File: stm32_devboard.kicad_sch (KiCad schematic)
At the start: 26 parts, among them J1 Conn_01x04_Male, J2 USB_B_Micro, SW1 SW_SPDT, U2 STM32F103CBT6, Y1 Crystal_GND24

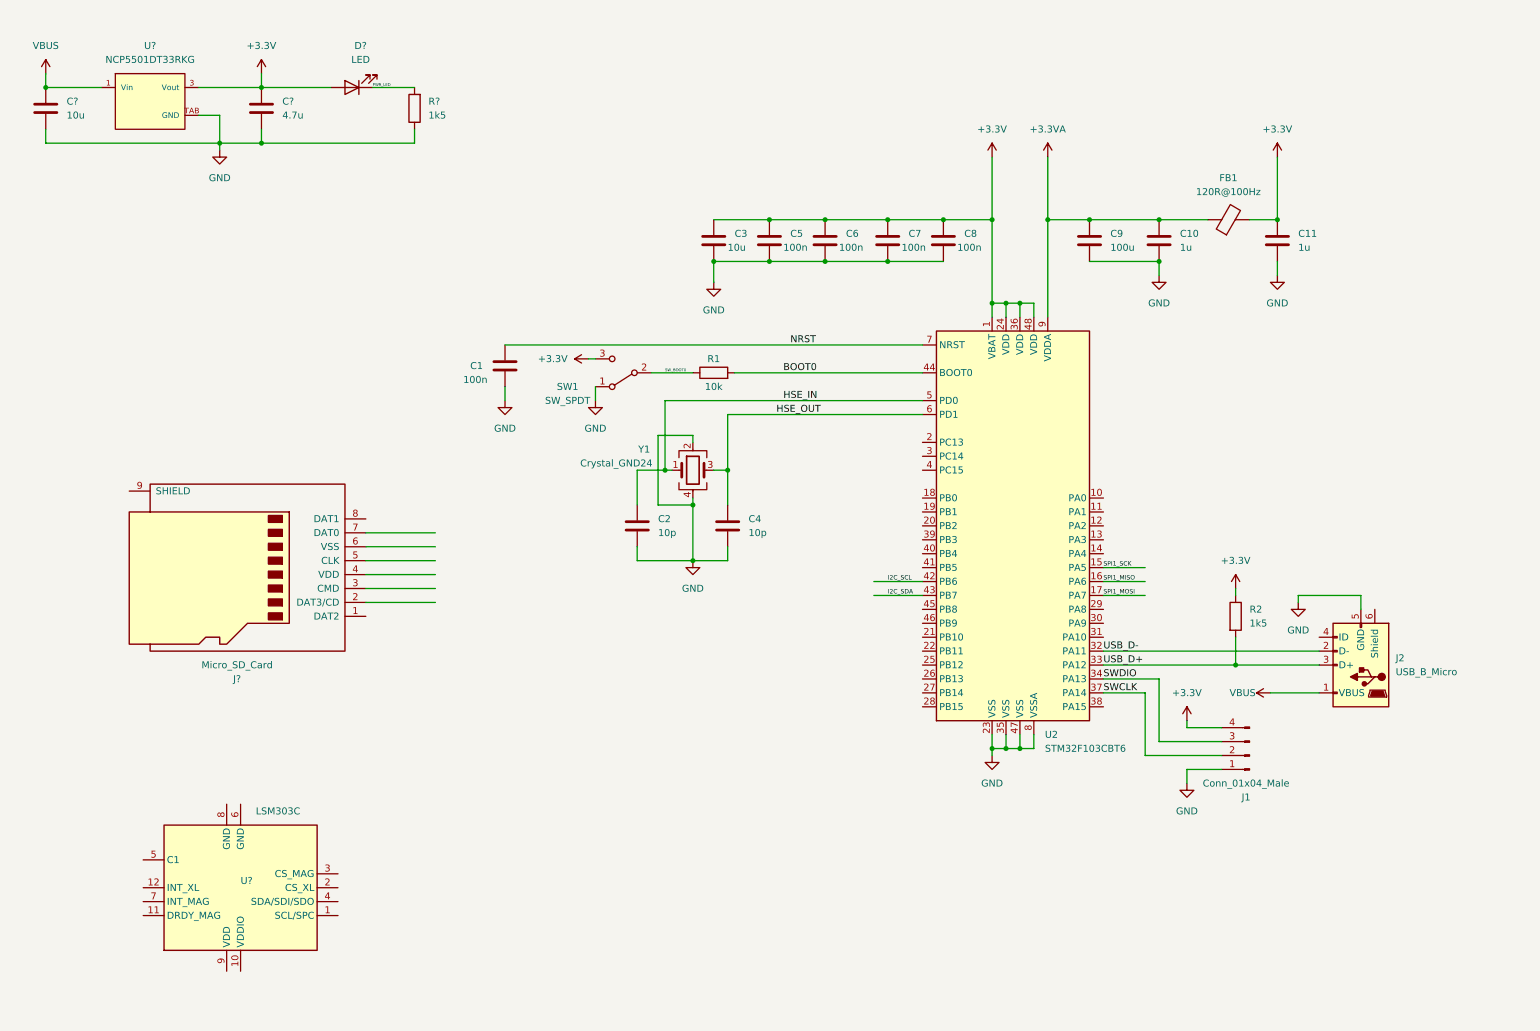
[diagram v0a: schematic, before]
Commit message: sd card schematic done
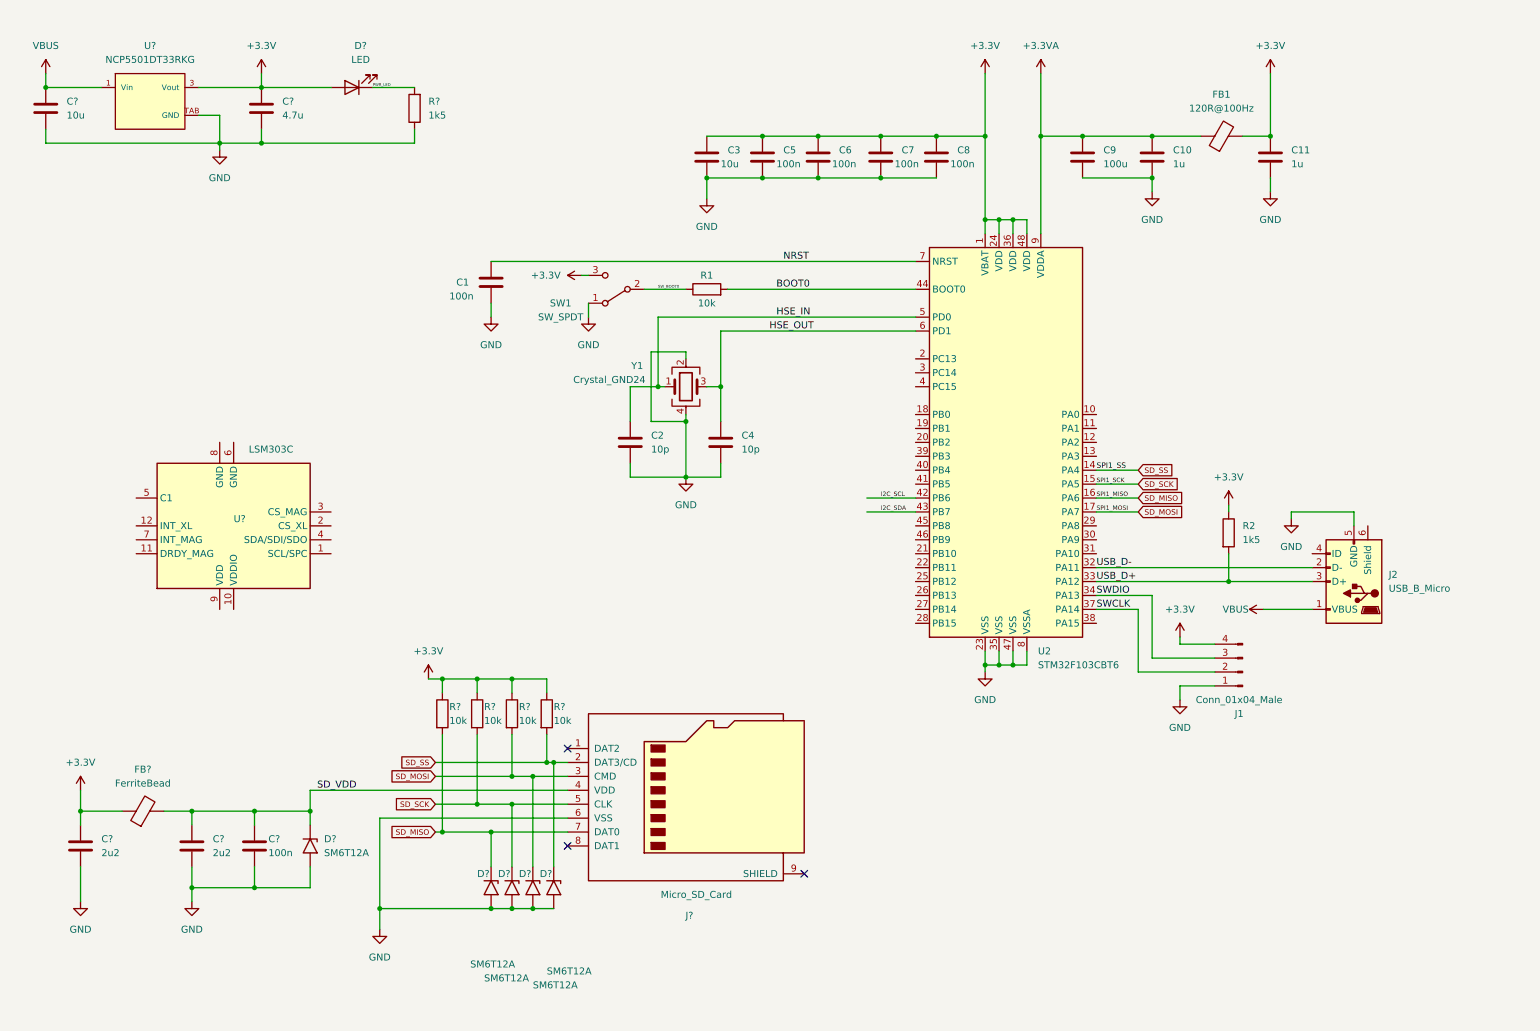
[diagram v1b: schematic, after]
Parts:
- added C?: 100n, symbol Device:C
- added C? (x2): 2u2, symbol Device:C
- added D? (x5): SM6T12A, Diode_SMD:D_SMB, symbol Diode:SM6T12A
- added FB?: FerriteBead, symbol Device:FerriteBead
- added R? (x4): 10k, symbol Device:R
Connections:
- net SPI1_MISO is gone; now on net SD_MISO: U2.16 (PA6)
- net SPI1_MOSI is gone; now on net SD_MOSI: U2.17 (PA7)
- net SPI1_SCK is gone; now on net SD_SCK: U2.15 (PA5)
- net +3V3: now also C?.1, FB?.1, R?.1, R?.1, R?.1, R?.1
- net GND: now also J?.6 (VSS), C?.2, C?.2, C?.2, D?.2 (A2), D?.2 (A2), D?.2 (A2), D?.2 (A2), D?.2 (A2)
- net SD_SS: now reaches U2.14 (PA4)
- net SD_SS: now also J?.2 (DAT3/CD), D?.1 (A1), R?.2
- net SD_MOSI: now reaches J?.3 (CMD)
- net SD_MOSI: now also D?.1 (A1), R?.2
- net SD_VDD: now reaches J?.4 (VDD)
- net SD_VDD: now also C?.1, C?.1, D?.1 (A1), FB?.2
- net SD_SCK: now reaches J?.5 (CLK)
- net SD_SCK: now also D?.1 (A1), R?.2
- net SD_MISO: now reaches J?.7 (DAT0)
- net SD_MISO: now also D?.1 (A1), R?.2
- no-connect marks 0 -> 3
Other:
- moved on the sheet: C1, C10, C11, C2, C3, C4, C5, C6, C7, C8, C9, FB1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

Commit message: add imu
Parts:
- added C? (x3): 100n, symbol Device:C
- added C?: 10u, symbol Device:C
- added R? (x2): 1k5, symbol Device:R
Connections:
- net I2C_SCL is gone; now on net IMU_SCL: U2.42 (PB6)
- net I2C_SDA is gone; now on net IMU_SDA: U2.43 (PB7)
- net SW_BOOT0 is gone; now on net BOOT0: R1.1, SW1.2 (B)
- net +3V3: now also U?.10 (VDDIO), U?.2 (CS_XL), U?.3 (CS_MAG), U?.9 (VDD), C?.1, C?.1, C?.1, R?.1, R?.1
- net BOOT0: no longer R1.2, U2.44 (BOOT0)
- net GND: now also U?.6 (GND), U?.8 (GND), C?.2, C?.2, C?.2, C?.2
- net IMU_SCL: now reaches U?.1 (SCL/SPC)
- net IMU_SCL: now also R?.2
- net IMU_SDA: now reaches U?.4 (SDA/SDI/SDO)
- net IMU_SDA: now also R?.2
- net at U?.5 (C1): now also C?.1
- new net: R1.2, U2.44 (BOOT0)
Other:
- moved on the sheet: C1, C2, C4, C?, D?, FB?, J?, R1, R?, SW1, U?, Y1

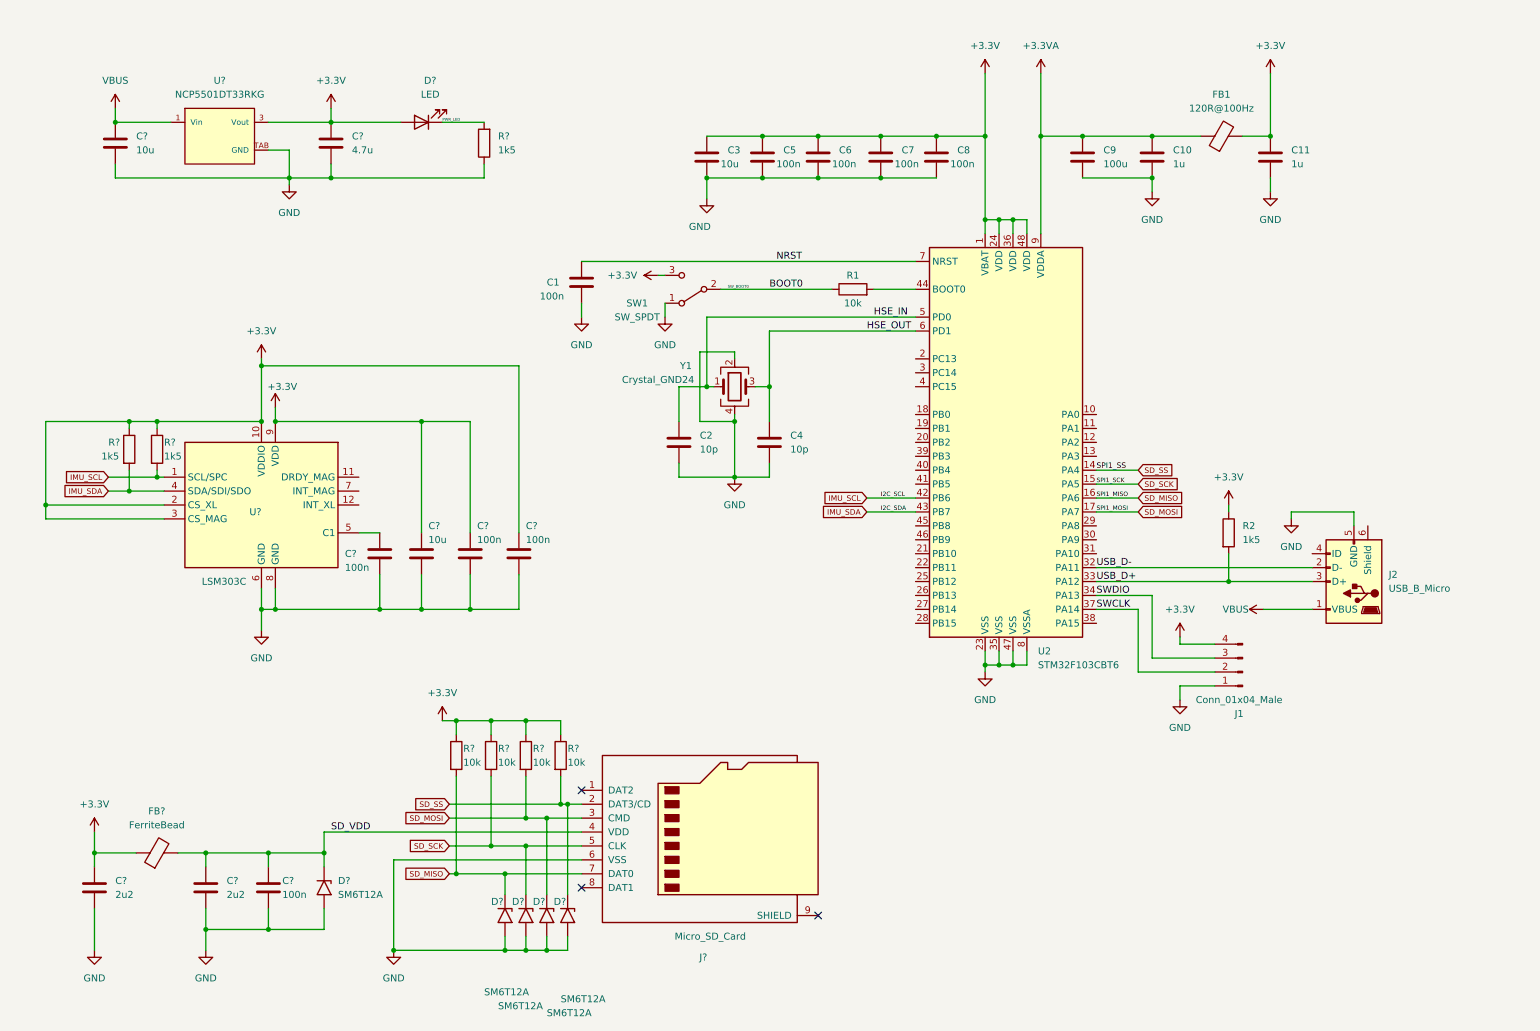
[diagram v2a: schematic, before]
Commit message: schematic annotation
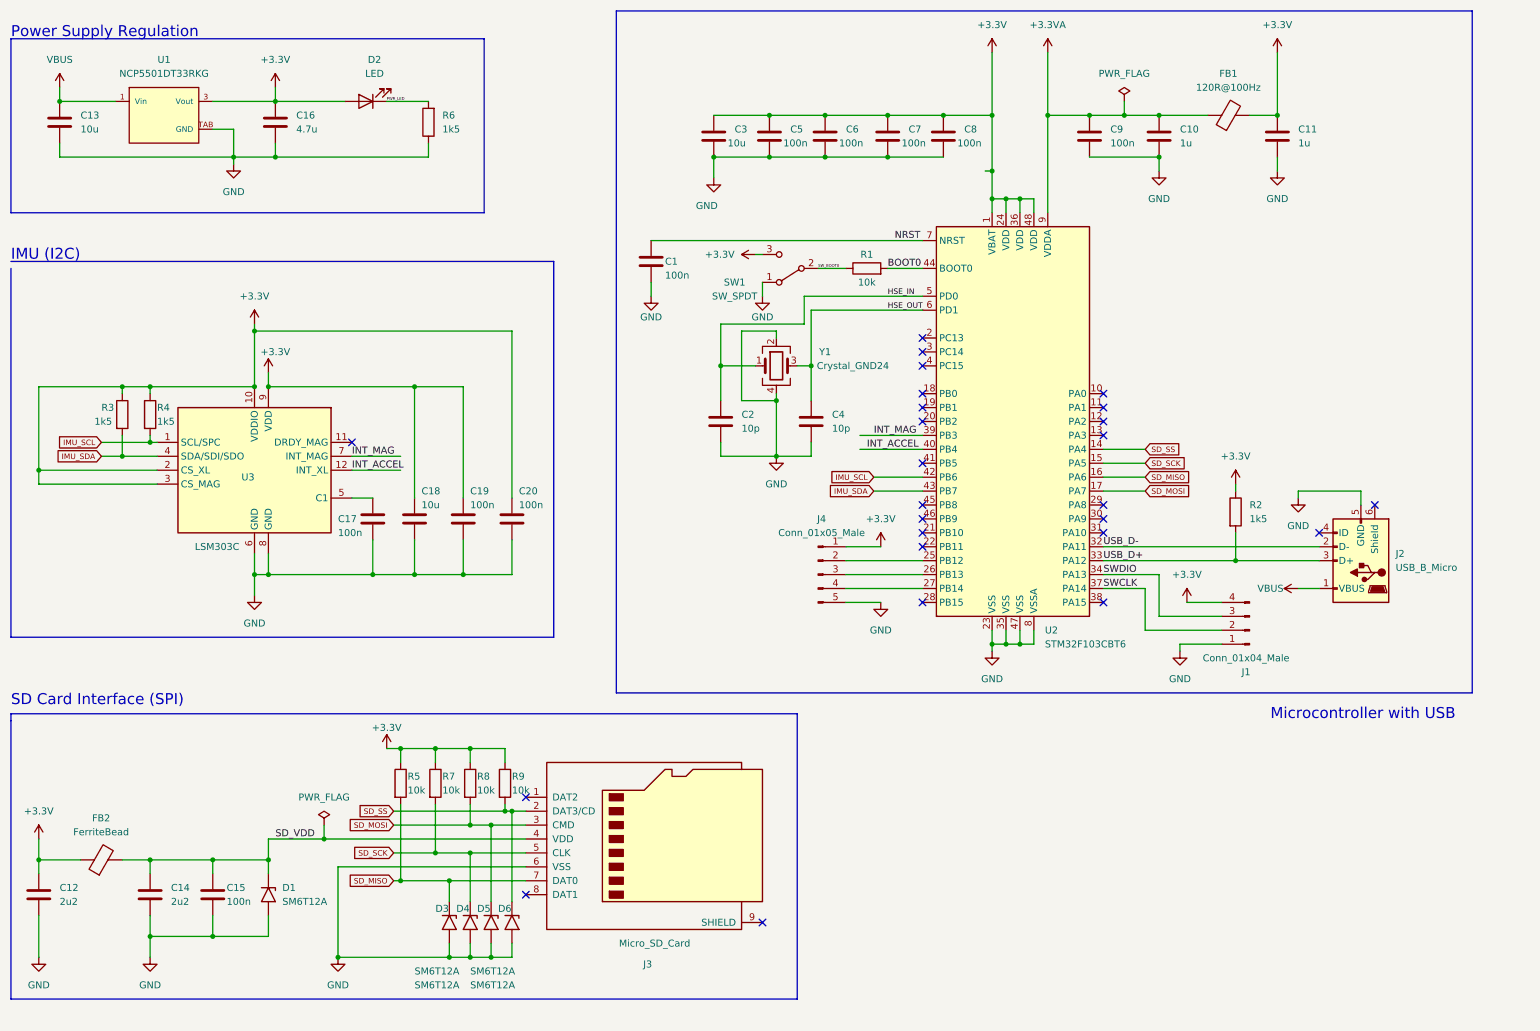
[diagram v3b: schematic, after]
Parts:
- added J4: Conn_01x05_Male, Connector_PinHeader_2.54mm:PinHeader_1x05_P2.54mm_Vertical, symbol Connector:Conn_01x05_Male
- C1, C10, C11, C2, C4, C5, C6, C7, C8: footprint (none) -> Capacitor_SMD:C_0402_1005Metric
- C12, C14, C15, C17, C19, C20: renamed from C?; footprint (none) -> Capacitor_SMD:C_0402_1005Metric
- C13, C16, C18: renamed from C?; footprint (none) -> Capacitor_SMD:C_0603_1608Metric
- C3: footprint (none) -> Capacitor_SMD:C_0603_1608Metric
- C9: value 100u -> 100n; footprint (none) -> Capacitor_SMD:C_0402_1005Metric
- D2: renamed from D?; footprint (none) -> LED_SMD:LED_0603_1608Metric
- FB1: footprint (none) -> Inductor_SMD:L_0603_1608Metric
- FB2: renamed from FB?; footprint (none) -> Inductor_SMD:L_0603_1608Metric
- J1: footprint (none) -> Connector_PinHeader_2.54mm:PinHeader_1x04_P2.54mm_Vertical
- J2: footprint (none) -> Connector_USB:USB_Micro-B_Wuerth_629105150521
- J3: renamed from J?; footprint (none) -> Connector_Card:microSD_HC_Wuerth_693072010801
- R1, R2: footprint (none) -> Resistor_SMD:R_0402_1005Metric
- R3, R4, R5, R6, R7, R8, R9: renamed from R?; footprint (none) -> Resistor_SMD:R_0402_1005Metric
- SW1: footprint (none) -> Button_Switch_THT:SW_E-Switch_EG1224_SPDT_Angled
- U3: renamed from U?; footprint (none) -> Package_LGA:LGA-12_2x2mm_P0.5mm
- Y1: footprint (none) -> Crystal:Crystal_SMD_3225-4Pin_3.2x2.5mm
- gave numbers to parts that had none: 6
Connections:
- net +3V3: now also J4.1 (Pin_1)
- net BOOT0: now also R1.2, U2.44 (BOOT0); no longer R1.1, SW1.2 (B)
- net GND: now also J4.5 (Pin_5)
- net at U2.25 (PB12): now also J4.2 (Pin_2)
- net at U2.26 (PB13): now also J4.3 (Pin_3)
- net at U2.27 (PB14): now also J4.4 (Pin_4)
- net INT_MAG: now reaches U2.39 (PB3)
- net INT_MAG: now also U3.7 (INT_MAG)
- net INT_ACCEL: now reaches U2.40 (PB4)
- net INT_ACCEL: now also U3.12 (INT_XL)
- new net SW_BOOT0: R1.1, SW1.2 (B)
- no-connect marks 3 -> 26
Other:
- note added: "IMU (I2C)"
- note added: "Microcontroller with USB"
- note added: "Power Supply Regulation"
- note added: "SD Card Interface (SPI)"
- company: (none) -> jesh
- title: (none) -> STM32 Devboard With On-Board IMU and SD Card Interface
- moved on the sheet: C1, C10, C11, C12, C13, C14, C15, C16, C17, C18, C19, C2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
